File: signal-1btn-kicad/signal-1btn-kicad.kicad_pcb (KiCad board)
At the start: 2 copper layers, 38.5 x 15 mm, 14 parts, among them SW1 SW_Push_DPDT

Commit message: Add texts, use 2×5 panel.
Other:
- board text added: "Návěstidlo Se v1.0 JH 2021"

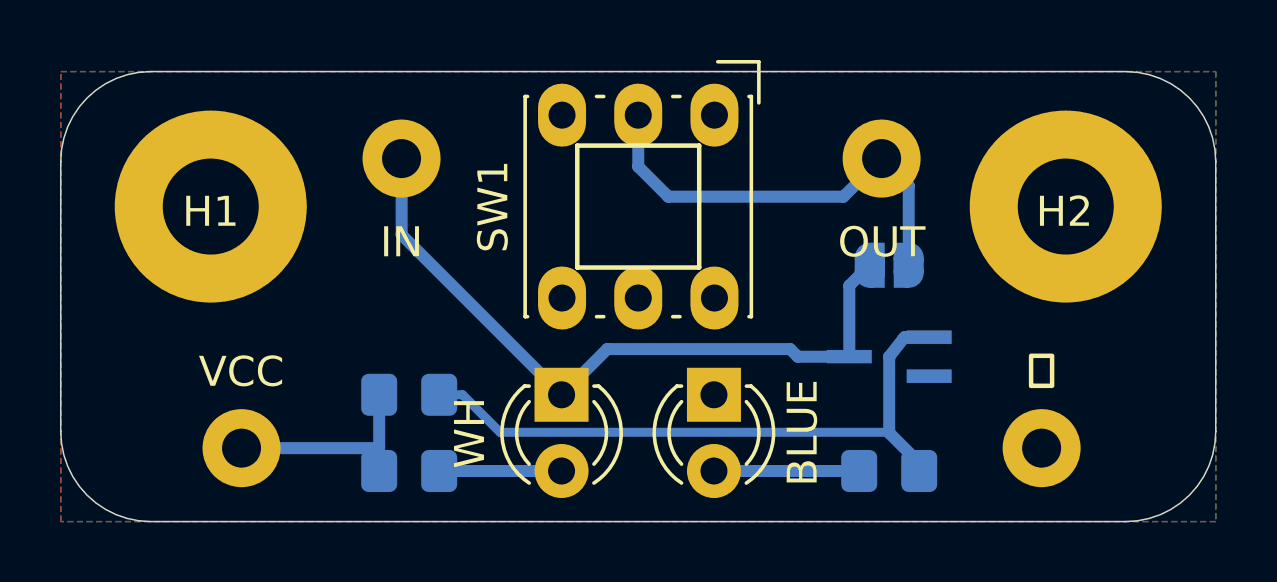
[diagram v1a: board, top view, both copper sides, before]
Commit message: Use mounting holes without Cu.
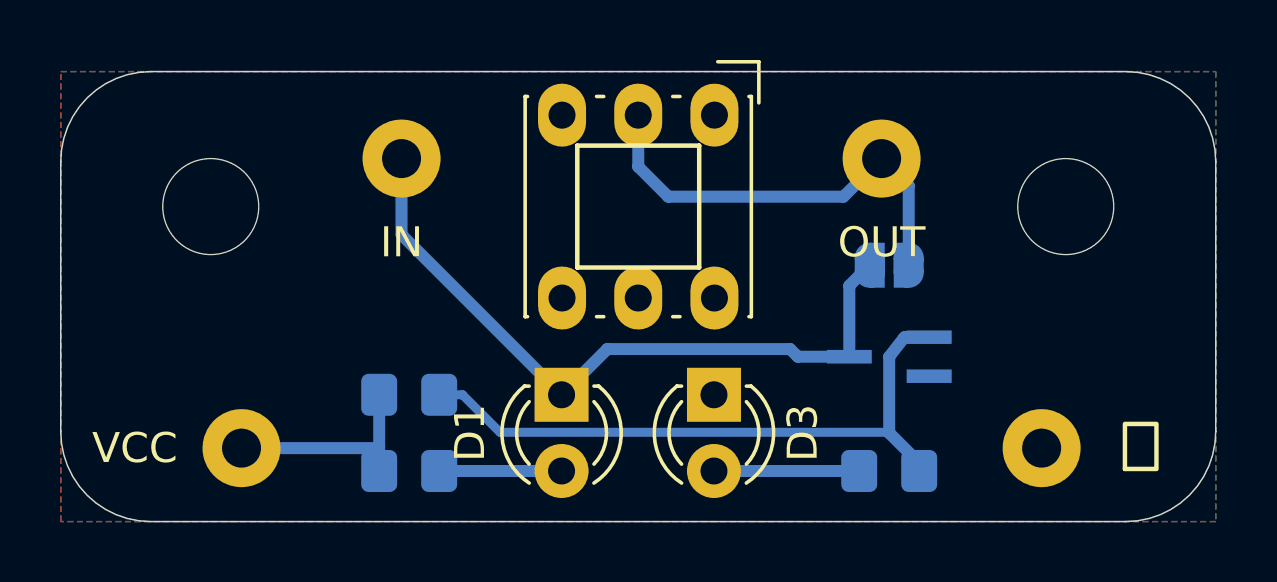
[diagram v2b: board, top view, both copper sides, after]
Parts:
- H1, H2: footprint MountingHole:MountingHole_3.2mm_M3_Pad -> MountingHole:MountingHole_3.2mm_M3
- turned H1 to 90 degrees
- renumbered ⏚ to CGND1, VCC to CVCC1, WH to D1, BLUE to D3
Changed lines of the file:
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@@
   (general
     (thickness 1.6)
-    (drawings 13)
+    (drawings 17)
     (tracks 29)
     (zones 0)
@@
     (add_net VCC)
   )
+  (module MountingHole:MountingHole_3.2mm_M3 (layer F.Cu)
+    (at 108.5 27)
+    (descr "Mounting Hole 3.2mm, no annular, M3")
+    (tags "mounting hole 3.2mm no annular m3")
+    (clearance 2)
+    (attr virtual)
+    (fp_text reference H2 (at 0 -4.2) (layer F.SilkS) hide
+      (effects (font (size 1 1) (thickness 0.15)))
+    )
+    (fp_text value MountingHole (at 0 4.2) (layer F.Fab)
+      (effects (font (size 1 1) (thickness 0.15)))
+    )
+    (fp_circle (center 0 0) (end 3.45 0) (layer F.CrtYd) (width 0.05))
+    (fp_circle (center 0 0) (end 3.2 0) (layer Cmts.User) (width 0.15))
+    (fp_text user %R (at 0.3 0) (layer F.Fab)
+      (effects (font (size 1 1) (thickness 0.15)))
+    )
+    (pad 1 np_thru_hole circle (at 0 0) (size 3.2 3.2) (drill 3.2) (layers *.Cu *.Mask))
+  )
+  (module MountingHole:MountingHole_3.2mm_M3 (layer F.Cu)
+    (at 80 27 90)
+    (descr "Mounting Hole 3.2mm, no annular, M3")
+    (tags "mounting hole 3.2mm no annular m3")
+    (clearance 2)
+    (attr virtual)
+    (fp_text reference H1 (at 0 -4.2 90) (layer F.SilkS) hide
+      (effects (font (size 1 1) (thickness 0.15)))
+    )
+    (fp_text value MountingHole (at 0 4.2 90) (layer F.Fab)
+      (effects (font (size 1 1) (thickness 0.15)))
+    )
+    (fp_circle (center 0 0) (end 3.45 0) (layer F.CrtYd) (width 0.05))
+    (fp_circle (center 0 0) (end 3.2 0) (layer Cmts.User) (width 0.15))
+    (fp_text user %R (at 0.3 0 90) (layer F.Fab)
+      (effects (font (size 1 1) (thickness 0.15)))
+    )
+    (pad 1 np_thru_hole circle (at 0 0 90) (size 3.2 3.2) (drill 3.2) (layers *.Cu *.Mask))
+  )
   (module LED_THT:LED_D3.0mm (layer F.Cu)
     (at 96.774 33.274 270)
     (descr "LED, diameter 3.0mm, 2 pins")
     (tags "LED diameter 3.0mm 2 pins")
-    (fp_text reference BLUE (at 1.27 -2.96 90) (layer F.SilkS)
+    (fp_text reference D3 (at 1.27 -2.96 90) (layer F.SilkS)
       (effects (font (size 1 1) (thickness 0.15)))
     )
@@
     (descr "solder Pin_ diameter 1.3mm, hole diameter 1.3mm, length 11.0mm")
     (tags "solder Pin_ pressfit")
-    (fp_text reference VCC (at -3.048 -2.032) (layer B.SilkS)
+    (fp_text reference CVCC1 (at -3.048 -2.032) (layer B.SilkS) hide
       (effects (font (size 1 1) (thickness 0.15)) (justify mirror))
     )
@@
     (descr "solder Pin_ diameter 1.3mm, hole diameter 1.3mm, length 11.0mm")
     (tags "solder Pin_ pressfit")
-    (fp_text reference OUT (at 2.794 -1.778) (layer B.SilkS)
+    (fp_text reference OUT (at 2.794 -1.778) (layer B.SilkS) hide
       (effects (font (size 1 1) (thickness 0.15)) (justify mirror))
     )
@@
     (descr "solder Pin_ diameter 1.3mm, hole diameter 1.3mm, length 11.0mm")
     (tags "solder Pin_ pressfit")
-    (fp_text reference IN (at 0 2.794) (layer B.SilkS)
+    (fp_text reference IN (at 0 2.794) (layer B.SilkS) hide
       (effects (font (size 1 1) (thickness 0.15)) (justify mirror))
     )
@@
     (descr "solder Pin_ diameter 1.3mm, hole diameter 1.3mm, length 11.0mm")
     (tags "solder Pin_ pressfit")
-    (fp_text reference ⏚ (at 2.286 -2.032) (layer B.SilkS)
+    (fp_text reference CGND1 (at 2.286 -2.032) (layer B.SilkS) hide
       (effects (font (size 1 1) (thickness 0.15)) (justify mirror))
     )
@@
     (descr "LED, diameter 3.0mm, 2 pins")
     (tags "LED diameter 3.0mm 2 pins")
-    (fp_text reference WH (at 1.27 3.048 90) (layer F.SilkS)
+    (fp_text reference D1 (at 1.27 3.048 90) (layer F.SilkS)
       (effects (font (size 1 1) (thickness 0.15)))
     )
@@
     )
   )
-  (module MountingHole:MountingHole_3.2mm_M3_Pad (layer F.Cu)
-    (at 108.5 27)
-    (descr "Mounting Hole 3.2mm, M3")
-    (tags "mounting hole 3.2mm m3")
-    (attr virtual)
-    (fp_text reference H2 (at -0.042 0.178) (layer F.SilkS)
-      (effects (font (size 1 1) (thickness 0.15)))
-    )
-    (fp_text value MountingHole (at 0 4.2) (layer F.Fab)
-      (effects (font (size 1 1) (thickness 0.15)))
-    )
-    (fp_circle (center 0 0) (end 3.45 0) (layer F.CrtYd) (width 0.05))
-    (fp_circle (center 0 0) (end 3.2 0) (layer Cmts.User) (width 0.15))
-    (fp_text user %R (at 0.3 0) (layer F.Fab)
-      (effects (font (size 1 1) (thickness 0.15)))
-    )
-    (pad 1 thru_hole circle (at 0 0) (size 6.4 6.4) (drill 3.2) (layers *.Cu *.Mask))
-  )
-  (module MountingHole:MountingHole_3.2mm_M3_Pad (layer F.Cu)
-    (at 80 27)
-    (descr "Mounting Hole 3.2mm, M3")
-    (tags "mounting hole 3.2mm m3")
-    (attr virtual)
-    (fp_text reference H1 (at 0 0.178) (layer F.SilkS)
-      (effects (font (size 1 1) (thickness 0.15)))
-    )
-    (fp_text value MountingHole (at 0 4.2) (layer F.Fab)
-      (effects (font (size 1 1) (thickness 0.15)))
-    )
-    (fp_circle (center 0 0) (end 3.45 0) (layer F.CrtYd) (width 0.05))
-    (fp_circle (center 0 0) (end 3.2 0) (layer Cmts.User) (width 0.15))
-    (fp_text user %R (at 0.3 0) (layer F.Fab)
-      (effects (font (size 1 1) (thickness 0.15)))
-    )
-    (pad 1 thru_hole circle (at 0 0) (size 6.4 6.4) (drill 3.2) (layers *.Cu *.Mask))
-  )
   (module Switch_KMZ:KLS7 (layer F.Cu)
     (at 94.25 27 270)
-    (fp_text reference SW1 (at 0 4.826 90) (layer F.SilkS)
+    (fp_text reference SW1 (at 0 4.826 90) (layer F.SilkS) hide
       (effects (font (size 1 1) (thickness 0.15)))
     )
@@
       ))
   )
+  (gr_text VCC (at 77.47 35.052) (layer B.SilkS)
+    (effects (font (size 1 1) (thickness 0.15)) (justify mirror))
+  )
+  (gr_text ⏚ (at 110.998 35.052) (layer B.SilkS)
+    (effects (font (size 1.5 1.5) (thickness 0.15)) (justify mirror))
+  )
+  (gr_text IN (at 86.36 28.194) (layer B.SilkS)
+    (effects (font (size 1 1) (thickness 0.15)) (justify mirror))
+  )
+  (gr_text OUT (at 105.156 23.622) (layer B.SilkS)
+    (effects (font (size 1 1) (thickness 0.15)) (justify mirror))
+  )
   (gr_text "Návěstidlo Se\nv1.0 JH 2021" (at 94.234 26.924) (layer B.SilkS)
     (effects (font (size 1 1) (thickness 0.15)) (justify mirror))
@@
     (effects (font (size 1 1) (thickness 0.15)))
   )
-  (gr_text ⏚ (at 107.696 32.512) (layer F.SilkS)
+  (gr_text ⏚ (at 110.998 35.052) (layer F.SilkS)
+    (effects (font (size 1.5 1.5) (thickness 0.15)))
+  )
+  (gr_text VCC (at 77.47 35.052) (layer F.SilkS)
     (effects (font (size 1 1) (thickness 0.15)))
   )
-  (gr_text VCC (at 81.026 32.512) (layer F.SilkS)
-    (effects (font (size 1 1) (thickness 0.15)))
-  )

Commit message: Fix BAT54 package (SOT23).
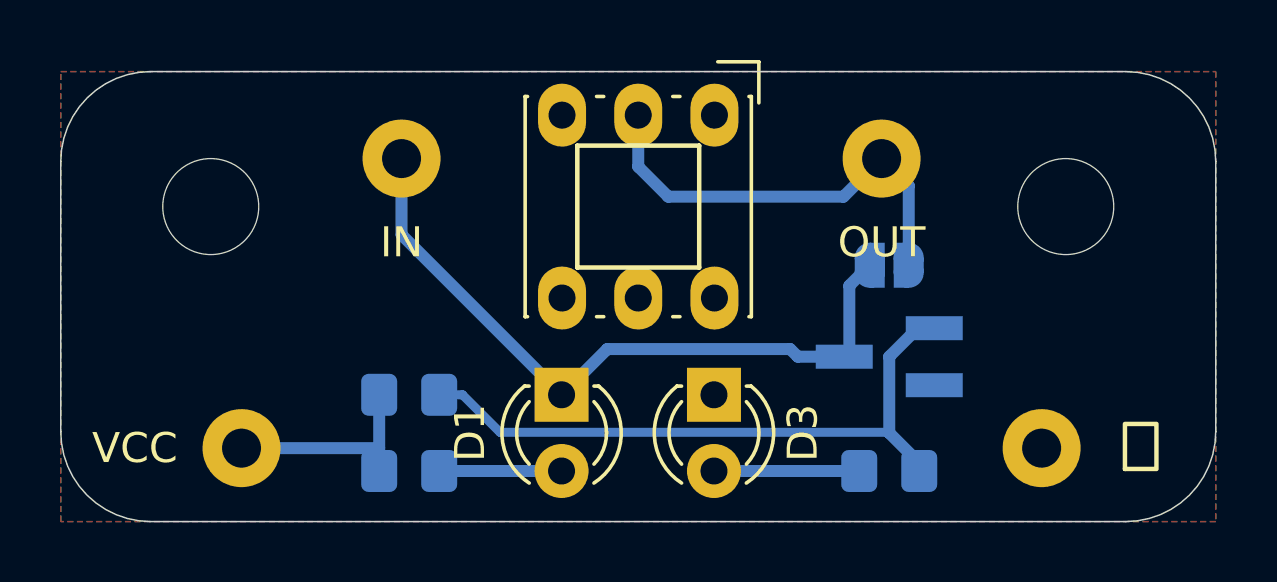
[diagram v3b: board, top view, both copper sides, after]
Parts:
- D2: footprint Package_TO_SOT_SMD:SOT-323_SC-70_Handsoldering -> Package_TO_SOT_SMD:SOT-23_Handsoldering
- renumbered IN to CINPUT1, OUT to COUTPUT1

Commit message: Signal: switch diodes.
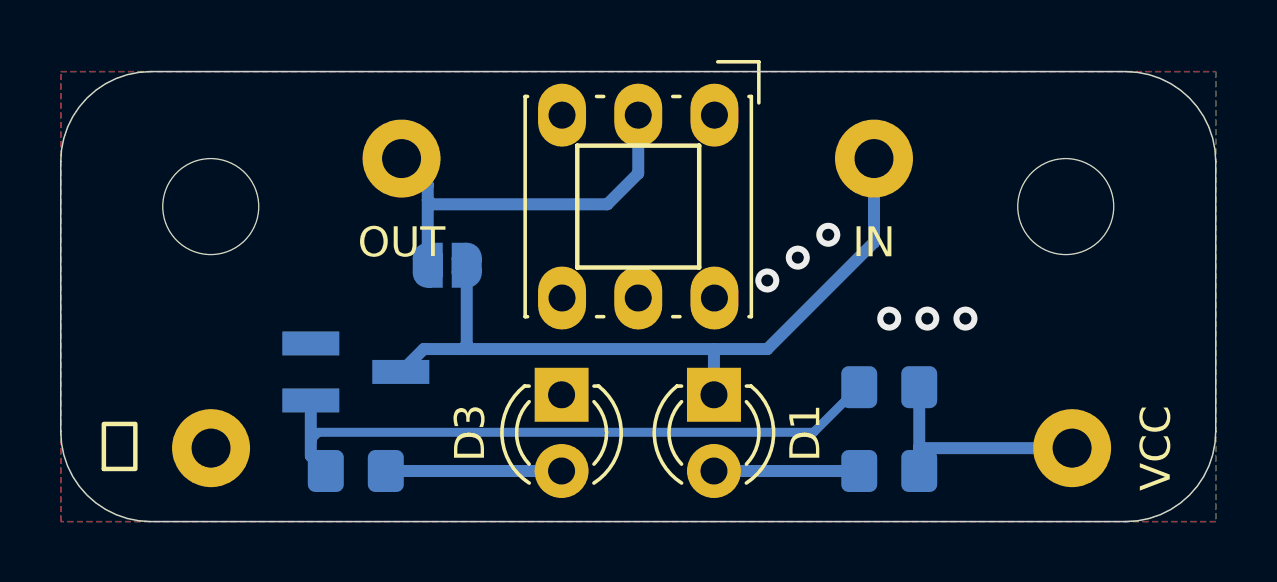
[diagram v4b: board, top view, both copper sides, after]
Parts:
- moved CVCC1 27.7 mm to (108.7, 35.1)
- moved CGND1 27.7 mm to (80.0, 35.1)
- moved D2 17.8 mm to (84.8, 32.5), turned to 0 degrees
- moved R3 17.8 mm to (84.8, 35.8), turned to 0 degrees
- moved R2 16.0 mm to (102.6, 33.0), turned to 180 degrees
- moved COUTPUT1 16.0 mm to (86.4, 25.4)
- moved R1 16.0 mm to (102.6, 35.8), turned to 180 degrees
- moved CINPUT1 15.7 mm to (102.1, 25.4)
- moved JP1 14.7 mm to (87.9, 29.0), turned to 180 degrees
- moved D1 5.08 mm to (96.8, 33.3)
- moved D3 5.08 mm to (91.7, 33.3)
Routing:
- net Net-(COUTPUT1-Pad1): track 16.0 -> 13.4 mm
- net Net-(D3-Pad2): track 4.84 -> 5.86 mm
- net Net-(CINPUT1-Pad1): track 23.7 -> 24.7 mm
- net Net-(D1-Pad2): track 4.08 -> 4.84 mm
- net VCC: track 7.13 -> 7.90 mm
- net GND: vias 0 -> 6
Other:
- board text added: "Návěstidlo Se v2.0 JH 2021"
- board text removed: "Návěstidlo Se v1.0 JH 2021"
